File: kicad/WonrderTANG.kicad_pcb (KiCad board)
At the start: 2 copper layers, 101.6 x 89.5 mm, 28 parts, among them CON1 MSX-CONNECTOR, J2 AudioJack3, J3 AUDIO, Q1 2N3904, Q2 2N3904, U1 SN74LVC245AN, U2 SN74LVC245AN, U3 SN74LVC245AN, U4 SN74LVC245AN, U5 Tang_Nano_20k, U6 SN74LVC245AN

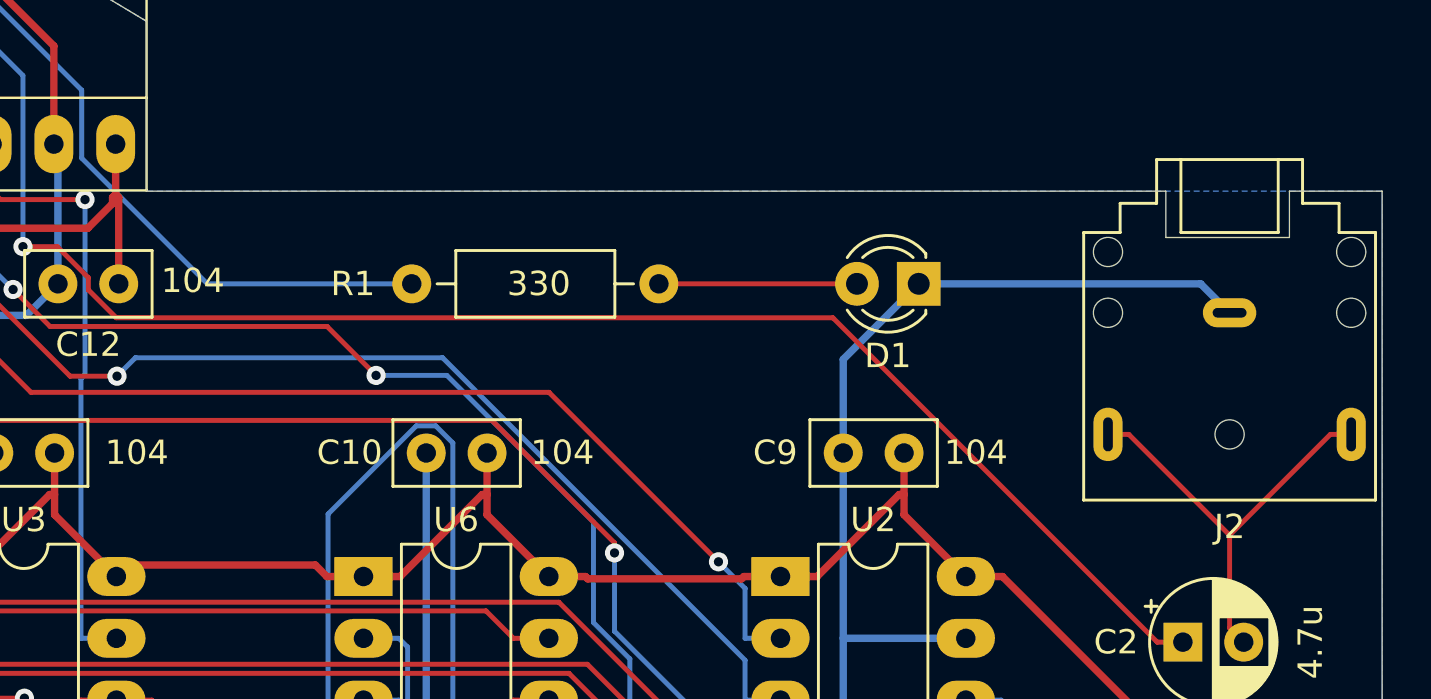
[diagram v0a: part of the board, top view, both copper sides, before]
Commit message: kicad: change audio connector from CP1-3523N to SJ1-3525N
Signed-off-by: Albert Herranz <albert_herranz@yahoo.es>
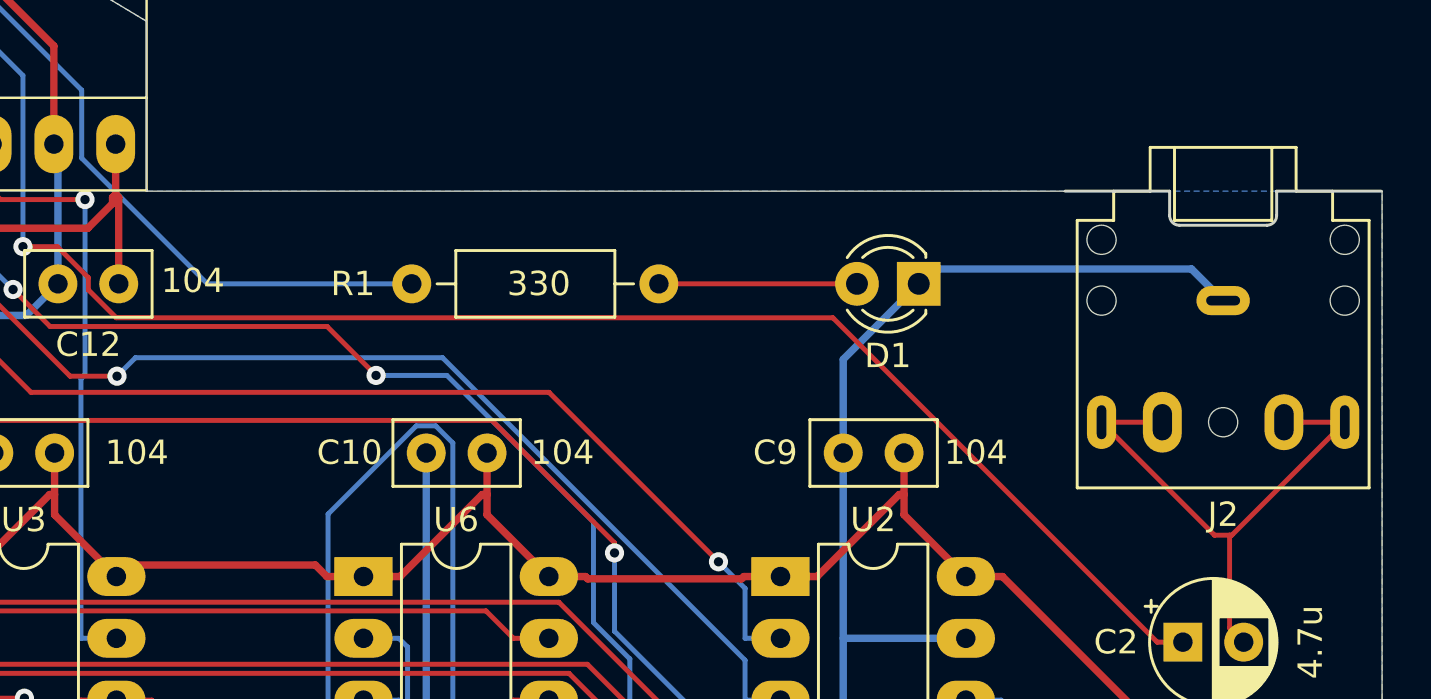
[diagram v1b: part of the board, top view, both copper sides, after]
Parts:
- J2: footprint Tang20K:SJ1-3523N -> Connector_Audio:Jack_3.5mm_CUI_SJ1-3525N_Horizontal
- moved J2 0.57 mm to (171.9, 68.0)
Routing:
- net Net-(C2-Pad2): track 18.1 -> 23.5 mm
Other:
- outline, holes or cut-outs redrawn
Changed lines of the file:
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@@
 		)
 	)
-	(footprint "Tang20K:SJ1-3523N"
+	(footprint "Connector_Audio:Jack_3.5mm_CUI_SJ1-3525N_Horizontal"
 		(layer "F.Cu")
-		(at 172.165 68.5 180)
+		(at 171.9 68 180)
 		(descr "TRS 3.5mm, horizontal, through-hole, https://www.cuidevices.com/product/resource/pdf/sj1-352xn.pdf")
 		(tags "TRS audio jack stereo horizontal")
@@
 			)
 		)
-		(property "Footprint" "Tang20K:SJ1-3523N"
+		(property "Footprint" "Connector_Audio:Jack_3.5mm_CUI_SJ1-3525N_Horizontal"
 			(at 0 0 180)
 			(unlocked yes)
@@
 			)
 		)
-		(property "Description" ""
+		(property "Description" "Audio Jack, 3 Poles (Stereo / TRS), Switched TR Poles (Normalling)"
 			(at 0 0 180)
 			(unlocked yes)
@@
 		)
 		(fp_line
+			(start 2.2 4.5)
+			(end 6.5 4.5)
+			(stroke
+				(width 0.12)
+				(type solid)
+			)
+			(layer "Edge.Cuts")
+		)
+		(fp_line
+			(start 2.2 3.5)
+			(end 2.2 4.5)
+			(stroke
+				(width 0.12)
+				(type solid)
+			)
+			(layer "Edge.Cuts")
+		)
+		(fp_line
+			(start 1.8 3.1)
+			(end -1.8 3.1)
+			(stroke
+				(width 0.12)
+				(type solid)
+			)
+			(layer "Edge.Cuts")
+		)
+		(fp_line
+			(start -2.2 4.5)
+			(end -6.5 4.5)
+			(stroke
+				(width 0.12)
+				(type solid)
+			)
+			(layer "Edge.Cuts")
+		)
+		(fp_line
+			(start -2.2 3.5)
+			(end -2.2 4.5)
+			(stroke
+				(width 0.12)
+				(type solid)
+			)
+			(layer "Edge.Cuts")
+		)
+		(fp_arc
+			(start 1.8 3.1)
+			(mid 2.082843 3.217157)
+			(end 2.2 3.5)
+			(stroke
+				(width 0.12)
+				(type solid)
+			)
+			(layer "Edge.Cuts")
+		)
+		(fp_arc
+			(start -2.2 3.5)
+			(mid -2.082842 3.217158)
+			(end -1.8 3.1)
+			(stroke
+				(width 0.12)
+				(type solid)
+			)
+			(layer "Edge.Cuts")
+		)
+		(fp_line
 			(start 6.25 4.75)
 			(end 6.25 4.5)
@@
 		)
 		(fp_line
-			(start 2.2 4.5)
-			(end 6.5 4.5)
-			(stroke
-				(width 0.12)
-				(type solid)
-			)
-			(layer "F.Fab")
-		)
-		(fp_line
-			(start 2.2 3.5)
-			(end 2.2 4.5)
-			(stroke
-				(width 0.12)
-				(type solid)
-			)
-			(layer "F.Fab")
-		)
-		(fp_line
-			(start 1.8 3.1)
-			(end -1.8 3.1)
-			(stroke
-				(width 0.12)
-				(type solid)
-			)
-			(layer "F.Fab")
-		)
-		(fp_line
-			(start -2.2 4.5)
-			(end -6.5 4.5)
-			(stroke
-				(width 0.12)
-				(type solid)
-			)
-			(layer "F.Fab")
-		)
-		(fp_line
-			(start -2.2 3.5)
-			(end -2.2 4.5)
-			(stroke
-				(width 0.12)
-				(type solid)
-			)
-			(layer "F.Fab")
-		)
-		(fp_line
 			(start -3 6.3)
 			(end 3 6.3)
@@
 			(layer "F.Fab")
 		)
-		(fp_arc
-			(start 1.8 3.1)
-			(mid 2.082843 3.217157)
-			(end 2.2 3.5)
-			(stroke
-				(width 0.12)
-				(type solid)
-			)
-			(layer "F.Fab")
-		)
-		(fp_arc
-			(start -2.2 3.5)
-			(mid -2.082842 3.217158)
-			(end -1.8 3.1)
-			(stroke
-				(width 0.12)
-				(type solid)
-			)
-			(layer "F.Fab")
-		)
 		(fp_text user "PCB edge"
 			(at 0 3.65 180)
@@
 			(pintype "passive")
 		)
+		(pad "RN" thru_hole oval
+			(at -2.5 -5 180)
+			(size 1.6 2.3)
+			(drill oval 0.8 1.5)
+			(layers "*.Cu" "*.Mask")
+			(remove_unused_layers no)
+			(net 82 "Net-(C2-Pad2)")
+			(pintype "passive")
+		)
 		(pad "S" thru_hole oval
 			(at 0 0 180)
@@
 			(pintype "passive")
 		)
-		(model "${KICAD8_3DMODEL_DIR}/Connector_Audio.3dshapes/Jack_3.5mm_CUI_SJ1-3523N_Horizontal.wrl"
+		(pad "TN" thru_hole oval
+			(at 2.5 -5)
+			(size 1.6 2.5)
+			(drill oval 0.8 1.5)
+			(layers "*.Cu" "*.Mask")
+			(remove_unused_layers no)
+			(net 82 "Net-(C2-Pad2)")
+			(pintype "passive")
+		)
+		(model "${KICAD8_3DMODEL_DIR}/Connector_Audio.3dshapes/Jack_3.5mm_CUI_SJ1-3525N_Horizontal.wrl"
 			(offset
 				(xyz 0 0 0)
@@
 	)
 	(gr_line
-		(start 174.625 63.5)
-		(end 174.625 65.405)
-		(stroke
-			(width 0.05)
-			(type default)
-		)
-		(layer "Edge.Cuts")
-	)
-	(gr_line
 		(start 127.635 46.355)
 		(end 127.635 39.37)
@@
 	)
 	(gr_line
-		(start 178.435 63.5)
-		(end 174.625 63.5)
-		(stroke
-			(width 0.05)
-			(type default)
-		)
-		(layer "Edge.Cuts")
-	)
-	(gr_line
 		(start 99.06 118.745)
 		(end 99.06 128.27)
@@
 	)
 	(gr_line
-		(start 174.625 65.405)
-		(end 169.545 65.405)
-		(stroke
-			(width 0.05)
-			(type default)
-		)
-		(layer "Edge.Cuts")
-	)
-	(gr_line
 		(start 124.46 48.26)
 		(end 127.635 46.355)
@@
 	)
 	(gr_line
-		(start 169.545 63.5)
+		(start 165.4 63.5)
 		(end 127.635 63.5)
 		(stroke
@@
 	)
 	(gr_line
-		(start 169.545 65.405)
-		(end 169.545 63.5)
+		(start 127.635 39.37)
+		(end 76.835 39.37)
 		(stroke
 			(width 0.05)
@@
 	)
 	(gr_line
-		(start 127.635 39.37)
-		(end 76.835 39.37)
+		(start 127.635 63.5)
+		(end 127.635 59.69)
 		(stroke
 			(width 0.05)
@@
 	)
 	(gr_line
-		(start 127.635 63.5)
-		(end 127.635 59.69)
+		(start 86.995 106.045)
+		(end 86.995 118.745)
 		(stroke
 			(width 0.05)
@@
 	)
 	(gr_line
-		(start 86.995 106.045)
-		(end 86.995 118.745)
+		(start 178.4 63.5)
+		(end 178.435 63.5)
 		(stroke
 			(width 0.05)
@@
 	)
 	(segment
-		(start 170.975 67.31)
-		(end 172.165 68.5)
-		(width 0.3048)
-		(locked yes)
-		(layer "B.Cu")
-		(net 2)
-	)
-	(segment
 		(start 87.025 74.265)
 		(end 87.025 99.665)
@@
 	)
 	(segment
+		(start 159.385 67.31)
+		(end 159.59 67.31)
+		(width 0.3048)
+		(layer "B.Cu")
+		(net 2)
+	)
+	(segment
 		(start 169.7795 101.3475)
 		(end 169.7795 108.123)
@@
 	)
 	(segment
+		(start 159.59 67.31)
+		(end 160.2 66.7)
+		(width 0.3048)
+		(locked yes)
+		(layer "B.Cu")
+		(net 2)
+	)
+	(segment
+		(start 160.2 66.7)
+		(end 170.6 66.7)
+		(width 0.3048)
+		(locked yes)
+		(layer "B.Cu")
+		(net 2)
+	)
+	(segment
 		(start 154.97 100.935)
 		(end 169.367 100.935)
@@
 	)
 	(segment
-		(start 159.385 67.31)
-		(end 170.975 67.31)
-		(width 0.3048)
-		(locked yes)
-		(layer "B.Cu")
-		(net 2)
-	)
-	(segment
 		(start 101.63 102.205)
 		(end 103.1365 102.205)
@@
 	)
 	(segment
+		(start 170.6 66.7)
+		(end 171.9 68)
+		(width 0.3048)
+		(locked yes)
+		(layer "B.Cu")
+		(net 2)
+	)
+	(segment
 		(start 79.435 49.022)
 		(end 79.435 49.463)
@@
 	)
 	(segment
+		(start 166.9 73)
+		(end 169.4 73)
+		(width 0.2032)
+		(layer "F.Cu")
+		(net 82)
+	)
+	(segment
 		(start 172.165 77.6443)
 		(end 172.165 81.4621)
@@
 	)
 	(segment
-		(start 177.165 73.5)
-		(end 176.3093 73.5)
+		(start 176.9 73)
+		(end 174.4 73)
 		(width 0.2032)
 		(layer "F.Cu")
@@
 	)
 	(segment
-		(start 176.3093 73.5)
-		(end 172.165 77.6443)
+		(start 172.165 77.6443)
+		(end 172.2557 77.6443)
+		(width 0.2032)
+		(layer "F.Cu")
+		(net 82)
+	)
+	(segment
+		(start 172.165 77.6443)
+		(end 171.5443 77.6443)
 		(width 0.2032)
 		(layer "F.Cu")
@@
 	)
 	(segment
-		(start 167.165 73.5)
-		(end 168.0207 73.5)
+		(start 172.2557 77.6443)
+		(end 176.9 73)
 		(width 0.2032)
 		(layer "F.Cu")
@@
 	)
 	(segment
-		(start 168.0207 73.5)
-		(end 172.165 77.6443)
+		(start 171.5443 77.6443)
+		(end 166.9 73)
 		(width 0.2032)
 		(layer "F.Cu")
